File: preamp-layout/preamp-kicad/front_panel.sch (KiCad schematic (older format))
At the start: 14 parts, among them J13 Conn_01x02_Male, J14 Conn_01x02_Female, J46 Conn_01x04_Female, SW10 SW_Push_Open, SW11 SW_Push_Open, SW4 SW_Push_Open, SW5 SW_Push_Open, SW6 SW_Push_Open, SW7 SW_Push_Open, SW8 SW_Push_Open, SW9 SW_Push_Open, U4 4021

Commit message: AC PCB Update
Removed Switch symbol from PCB, moved to main sheet. Started playing with footprint assignment. Other minor updates.
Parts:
- renumbered J13 to J17, J14 to J18, J46 to J19
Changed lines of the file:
@@
 AR Path="/5E5EF2D4/60B80487" Ref="J?"  Part="1"
 AR Path="/6009D432/60B80487" Ref="J?"  Part="1"
-AR Path="/5E5ECAAE/60B80487" Ref="J13"  Part="1"
-F 0 "J13" H 1522 6428 50  0000 R CNN
+AR Path="/5E5ECAAE/60B80487" Ref="J17"  Part="1"
+F 0 "J17" H 1522 6428 50  0000 R CNN
 F 1 "Conn_01x02_Male" H 1522 6383 50  0001 R CNN
 F 2 "" H 1550 6500 50  0001 C CNN
@@
 P 1550 7050
 AR Path="/6009D432/60B804B3" Ref="J?"  Part="1"
-AR Path="/5E5ECAAE/60B804B3" Ref="J14"  Part="1"
-F 0 "J14" H 1578 6980 50  0000 L CNN
+AR Path="/5E5ECAAE/60B804B3" Ref="J18"  Part="1"
+F 0 "J18" H 1578 6980 50  0000 L CNN
 F 1 "Conn_01x02_Female" H 1578 6935 50  0001 L CNN
 F 2 "" H 1550 7050 50  0001 C CNN
@@
 NoConn ~ 10500 4050
 $Comp
-L Connector:Conn_01x04_Female J46
+L Connector:Conn_01x04_Female J19
 U 1 1 65AE66F9
 P 10150 2800
-F 0 "J46" H 10178 2730 50  0000 L CNN
+F 0 "J19" H 10178 2730 50  0000 L CNN
 F 1 "Conn_01x04_Female" H 10178 2685 50  0001 L CNN
 F 2 "" H 10150 2800 50  0001 C CNN

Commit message: Transformer specification
updated schematic, BOM with power transformer info. Other minor schematic tweaks.
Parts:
- removed J18: Conn_01x02_Female, symbol Connector:Conn_01x02_Female
- added J18: Conn_01x02_Male, Connector_JST:JST_EH_B2B-EH-A_1x02_P2.50mm_Vertical, symbol Connector:Conn_01x02_Male
- J17: footprint (none) -> Connector_JST:JST_EH_B2B-EH-A_1x02_P2.50mm_Vertical
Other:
- moved on the sheet: J19
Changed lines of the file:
@@
 L 4xxx:4021 U4
 U 1 1 639BBE1A
-P 10100 4550
-F 0 "U4" H 10100 5531 50  0000 C CNN
-F 1 "4021" H 10100 5440 50  0000 C CNN
-F 2 "" H 10100 4700 50  0001 C CNN
-F 3 "https://assets.nexperia.com/documents/data-sheet/HEF4021B.pdf" H 10100 4700 50  0001 C CNN
-	1    10100 4550
-	1    0    0    -1
-$EndComp
-Text GLabel 10100 3450 1    50   UnSpc ~ 0
-+5V
-Wire Wire Line
-	10100 3750 10100 3450
-Text Label 9550 4450 2    50   ~ 0
+P 9500 4400
+F 0 "U4" H 9500 5381 50  0000 C CNN
+F 1 "4021" H 9500 5290 50  0000 C CNN
+F 2 "" H 9500 4550 50  0001 C CNN
+F 3 "https://assets.nexperia.com/documents/data-sheet/HEF4021B.pdf" H 9500 4550 50  0001 C CNN
+	1    9500 4400
+	1    0    0    -1
+$EndComp
+Text GLabel 9500 3300 1    50   UnSpc ~ 0
++5V
+Wire Wire Line
+	9500 3600 9500 3300
+Text Label 8950 4300 2    50   ~ 0
 SW_CH1
-Text Label 9550 4550 2    50   ~ 0
+Text Label 8950 4400 2    50   ~ 0
 SW_CH2
-Text Label 9550 4650 2    50   ~ 0
+Text Label 8950 4500 2    50   ~ 0
 SW_CH3
-Text Label 9550 4750 2    50   ~ 0
+Text Label 8950 4600 2    50   ~ 0
 SW_CH4
-Text Label 9550 4850 2    50   ~ 0
+Text Label 8950 4700 2    50   ~ 0
 SW_CH5
-Text Label 9550 4950 2    50   ~ 0
+Text Label 8950 4800 2    50   ~ 0
 SW_MUTE
 Wire Wire Line
-	9700 4450 9550 4450
-Wire Wire Line
-	9550 4650 9700 4650
-Wire Wire Line
-	9550 4550 9700 4550
-Wire Wire Line
-	9700 4750 9550 4750
-Wire Wire Line
-	9700 4850 9550 4850
-Wire Wire Line
-	9700 4950 9550 4950
-Text HLabel 10650 4150 2    50   Output ~ 0
+	9100 4300 8950 4300
+Wire Wire Line
+	8950 4500 9100 4500
+Wire Wire Line
+	8950 4400 9100 4400
+Wire Wire Line
+	9100 4600 8950 4600
+Wire Wire Line
+	9100 4700 8950 4700
+Wire Wire Line
+	9100 4800 8950 4800
+Text HLabel 10050 4000 2    50   Output ~ 0
 MISO
-Text HLabel 9550 4250 0    50   Input ~ 0
+Text HLabel 8950 4100 0    50   Input ~ 0
 MOSI
-Text HLabel 9550 3950 0    50   Input ~ 0
+Text HLabel 8950 3800 0    50   Input ~ 0
 CLK
-Text HLabel 9550 4150 0    50   Input ~ 0
+Text HLabel 8950 4000 0    50   Input ~ 0
 CS
 Wire Wire Line
-	9550 4250 9700 4250
-Wire Wire Line
-	9550 4150 9700 4150
-Wire Wire Line
-	9550 3950 9700 3950
-Wire Wire Line
-	10500 4150 10650 4150
+	8950 4100 9100 4100
+Wire Wire Line
+	8950 4000 9100 4000
+Wire Wire Line
+	8950 3800 9100 3800
+Wire Wire Line
+	9900 4000 10050 4000
 Text Label 5150 2650 3    50   ~ 0
 SW_CH1
@@
 Text Label 7550 2650 3    50   ~ 0
 SW_OUT_2
-Text Label 9550 5050 2    50   ~ 0
+Text Label 8950 4900 2    50   ~ 0
 SW_OUT_1
-Text Label 9550 5150 2    50   ~ 0
+Text Label 8950 5000 2    50   ~ 0
 SW_OUT_2
 Wire Wire Line
-	9700 5050 9550 5050
-Wire Wire Line
-	9550 5150 9700 5150
+	9100 4900 8950 4900
+Wire Wire Line
+	8950 5000 9100 5000
 Text GLabel 2100 1800 1    50   UnSpc ~ 0
 +5V
@@
 F 0 "J17" H 1522 6428 50  0000 R CNN
 F 1 "Conn_01x02_Male" H 1522 6383 50  0001 R CNN
-F 2 "" H 1550 6500 50  0001 C CNN
+F 2 "Connector_JST:JST_EH_B2B-EH-A_1x02_P2.50mm_Vertical" H 1550 6500 50  0001 C CNN
 F 3 "~" H 1550 6500 50  0001 C CNN
 	1    1550 6500
@@
 Wire Wire Line
 	1350 7050 1150 7050
-$Comp
-L Connector:Conn_01x02_Female J?
-U 1 1 60B804B3
-P 1550 7050
-AR Path="/6009D432/60B804B3" Ref="J?"  Part="1"
-AR Path="/5E5ECAAE/60B804B3" Ref="J18"  Part="1"
-F 0 "J18" H 1578 6980 50  0000 L CNN
-F 1 "Conn_01x02_Female" H 1578 6935 50  0001 L CNN
-F 2 "" H 1550 7050 50  0001 C CNN
-F 3 "~" H 1550 7050 50  0001 C CNN
-	1    1550 7050
-	1    0    0    -1
-$EndComp
 $Comp
 L power:GND #PWR?
@@
 L power:GND #PWR?
 U 1 1 64EC7570
-P 10100 5350
+P 9500 5200
 AR Path="/5E26F6FE/64EC7570" Ref="#PWR?"  Part="1"
 AR Path="/5E5ECAAE/64EC7570" Ref="#PWR023"  Part="1"
-F 0 "#PWR023" H 10100 5100 50  0001 C CNN
-F 1 "GND" H 10105 5177 50  0000 C CNN
-F 2 "" H 10100 5350 50  0001 C CNN
-F 3 "" H 10100 5350 50  0001 C CNN
-	1    10100 5350
-	1    0    0    -1
-$EndComp
-NoConn ~ 10500 3950
-NoConn ~ 10500 4050
+F 0 "#PWR023" H 9500 4950 50  0001 C CNN
+F 1 "GND" H 9505 5027 50  0000 C CNN
+F 2 "" H 9500 5200 50  0001 C CNN
+F 3 "" H 9500 5200 50  0001 C CNN
+	1    9500 5200
+	1    0    0    -1
+$EndComp
+NoConn ~ 9900 3800
+NoConn ~ 9900 3900
 $Comp
 L Connector:Conn_01x04_Female J19
 U 1 1 65AE66F9
-P 10150 2800
-F 0 "J19" H 10178 2730 50  0000 L CNN
-F 1 "Conn_01x04_Female" H 10178 2685 50  0001 L CNN
-F 2 "" H 10150 2800 50  0001 C CNN
-F 3 "~" H 10150 2800 50  0001 C CNN
-	1    10150 2800
-	1    0    0    -1
-$EndComp
-Text HLabel 9950 2900 0    50   Output ~ 0
+P 9550 2650
+F 0 "J19" H 9578 2580 50  0000 L CNN
+F 1 "Conn_01x04_Female" H 9578 2535 50  0001 L CNN
+F 2 "" H 9550 2650 50  0001 C CNN
+F 3 "~" H 9550 2650 50  0001 C CNN
+	1    9550 2650
+	1    0    0    -1
+$EndComp
+Text HLabel 9350 2750 0    50   Output ~ 0
 MISO
-Text HLabel 9950 2700 0    50   Input ~ 0
+Text HLabel 9350 2550 0    50   Input ~ 0
 CLK
-Text HLabel 9950 2800 0    50   Input ~ 0
+Text HLabel 9350 2650 0    50   Input ~ 0
 MOSI
-Text HLabel 9950 3000 0    50   Input ~ 0
+Text HLabel 9350 2850 0    50   Input ~ 0
 CS
+$Comp
+L Connector:Conn_01x02_Male J?
+U 1 1 5E8B15E1
+P 1550 7050
+AR Path="/5E5EF2D4/5E8B15E1" Ref="J?"  Part="1"
+AR Path="/6009D432/5E8B15E1" Ref="J?"  Part="1"
+AR Path="/5E5ECAAE/5E8B15E1" Ref="J18"  Part="1"
+F 0 "J18" H 1522 6978 50  0000 R CNN
+F 1 "Conn_01x02_Male" H 1522 6933 50  0001 R CNN
+F 2 "Connector_JST:JST_EH_B2B-EH-A_1x02_P2.50mm_Vertical" H 1550 7050 50  0001 C CNN
+F 3 "~" H 1550 7050 50  0001 C CNN
+	1    1550 7050
+	-1   0    0    -1
+$EndComp
 $EndSCHEMATC

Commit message: Added front panel LED sheet. BOM update. Front panel PCA work
other minor changes like LED color assignments, etc
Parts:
- removed D12, D13: WS2812B, LED_SMD:LED_WS2812B_PLCC4_5.0x5.0mm_P3.2mm, symbol LED:WS2812B
- removed J19: Conn_01x04_Female, symbol Connector:Conn_01x04_Female
- removed SW10, SW11, SW4, SW5, SW6, SW7, SW8, SW9: SW_Push_Open, symbol Switch:SW_Push_Open
- removed U4: 4021, symbol 4xxx:4021
- added C37, C38, C39, C40, C41, C42, C43, C44: 0.1uF, Capacitor_SMD:C_1206_3216Metric_Pad1.42x1.75mm_HandSolder, symbol Device:C
- added D60: RED, LED_SMD:LED_1206_3216Metric_Pad1.42x1.75mm_HandSolder, symbol Device:LED
- added J19: Conn_01x05_Female, symbol Connector:Conn_01x05_Female
- added J72, J73, J74, J75, J76, J77, J78, J79: Conn_01x03_Female, Connector_PinHeader_2.54mm:PinHeader_1x03_P2.54mm_Vertical, symbol Connector:Conn_01x03_Female
- added R87, R88, R89, R90, R91, R92, R93, R94: 100R, Resistor_SMD:R_1206_3216Metric_Pad1.42x1.75mm_HandSolder, symbol Device:R
- added R95: 430, Resistor_SMD:R_1206_3216Metric_Pad1.42x1.75mm_HandSolder, symbol Device:R
- added U4: MC33978, symbol preamp:MC33978
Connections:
- net labels added: SW_1, SW_2, SW_3, SW_4, SW_5, SW_6, SW_7, SW_8, SW_INT, SW_IN_1, SW_IN_2, SW_IN_3, SW_IN_4, SW_IN_5
- net labels removed: LED_DT, SW_CH1, SW_CH2, SW_CH3, SW_CH4, SW_CH5
- wire segments 21 -> 122
- no-connect marks 2 -> 16
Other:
- moved on the sheet: J17, J18

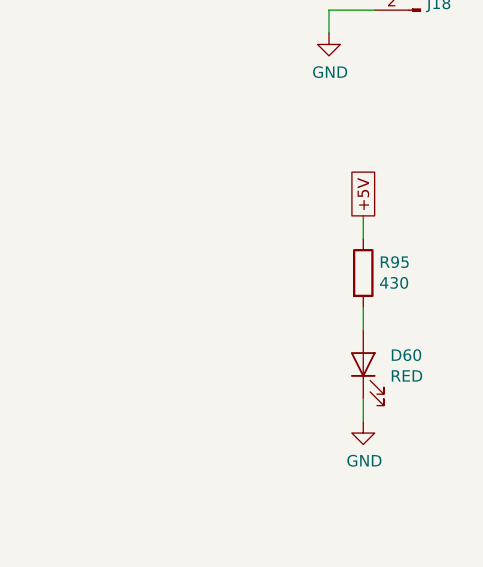
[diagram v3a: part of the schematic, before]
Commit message: LED resistor update
In the process of reviewing layouts and associated parts sourcing, I realized that I had incorrectly calculated the resistors needed for the power supply LEDs on all boards. Updated BOM and schematics to match. Other minor schematic updates.
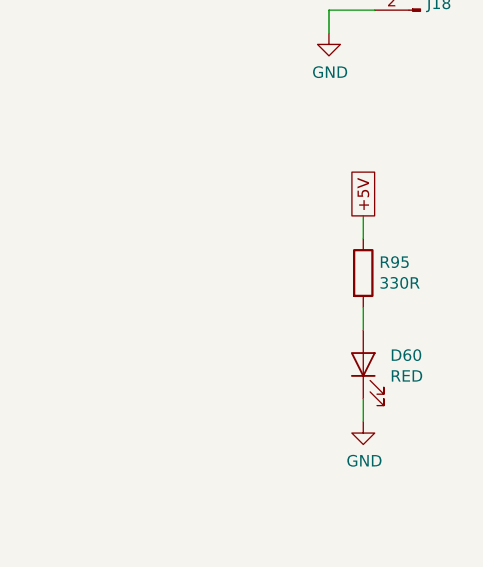
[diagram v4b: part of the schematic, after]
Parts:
- R95: value 430 -> 330R
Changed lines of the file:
@@
 Connection ~ 3600 5950
-$Comp
-L Device:R R?
-U 1 1 5ECB89C1
-P 9650 4600
-AR Path="/5E2D8DA2/5ECB89C1" Ref="R?"  Part="1"
-AR Path="/5ECB89C1" Ref="R?"  Part="1"
-AR Path="/5E27B612/5ECB89C1" Ref="R?"  Part="1"
-AR Path="/5E5EF2D4/5ECB89C1" Ref="R?"  Part="1"
-AR Path="/5E5ECAAE/5ECB89C1" Ref="R95"  Part="1"
-F 0 "R95" H 9720 4646 50  0000 L CNN
-F 1 "430" H 9720 4555 50  0000 L CNN
-F 2 "Resistor_SMD:R_1206_3216Metric_Pad1.42x1.75mm_HandSolder" V 9580 4600 50  0001 C CNN
-F 3 "~" H 9650 4600 50  0001 C CNN
-	1    9650 4600
-	1    0    0    -1
-$EndComp
 $Comp
 L Device:LED D?
@@
 Wire Wire Line
 	3600 5750 3600 5950
+$Comp
+L Device:R R?
+U 1 1 5ECB89C1
+P 9650 4600
+AR Path="/5E2D8DA2/5ECB89C1" Ref="R?"  Part="1"
+AR Path="/5ECB89C1" Ref="R?"  Part="1"
+AR Path="/5E27B612/5ECB89C1" Ref="R?"  Part="1"
+AR Path="/5E5EF2D4/5ECB89C1" Ref="R?"  Part="1"
+AR Path="/5E5ECAAE/5ECB89C1" Ref="R95"  Part="1"
+F 0 "R95" H 9720 4646 50  0000 L CNN
+F 1 "330R" H 9720 4555 50  0000 L CNN
+F 2 "Resistor_SMD:R_1206_3216Metric_Pad1.42x1.75mm_HandSolder" V 9580 4600 50  0001 C CNN
+F 3 "~" H 9650 4600 50  0001 C CNN
+	1    9650 4600
+	1    0    0    -1
+$EndComp
 $EndSCHEMATC

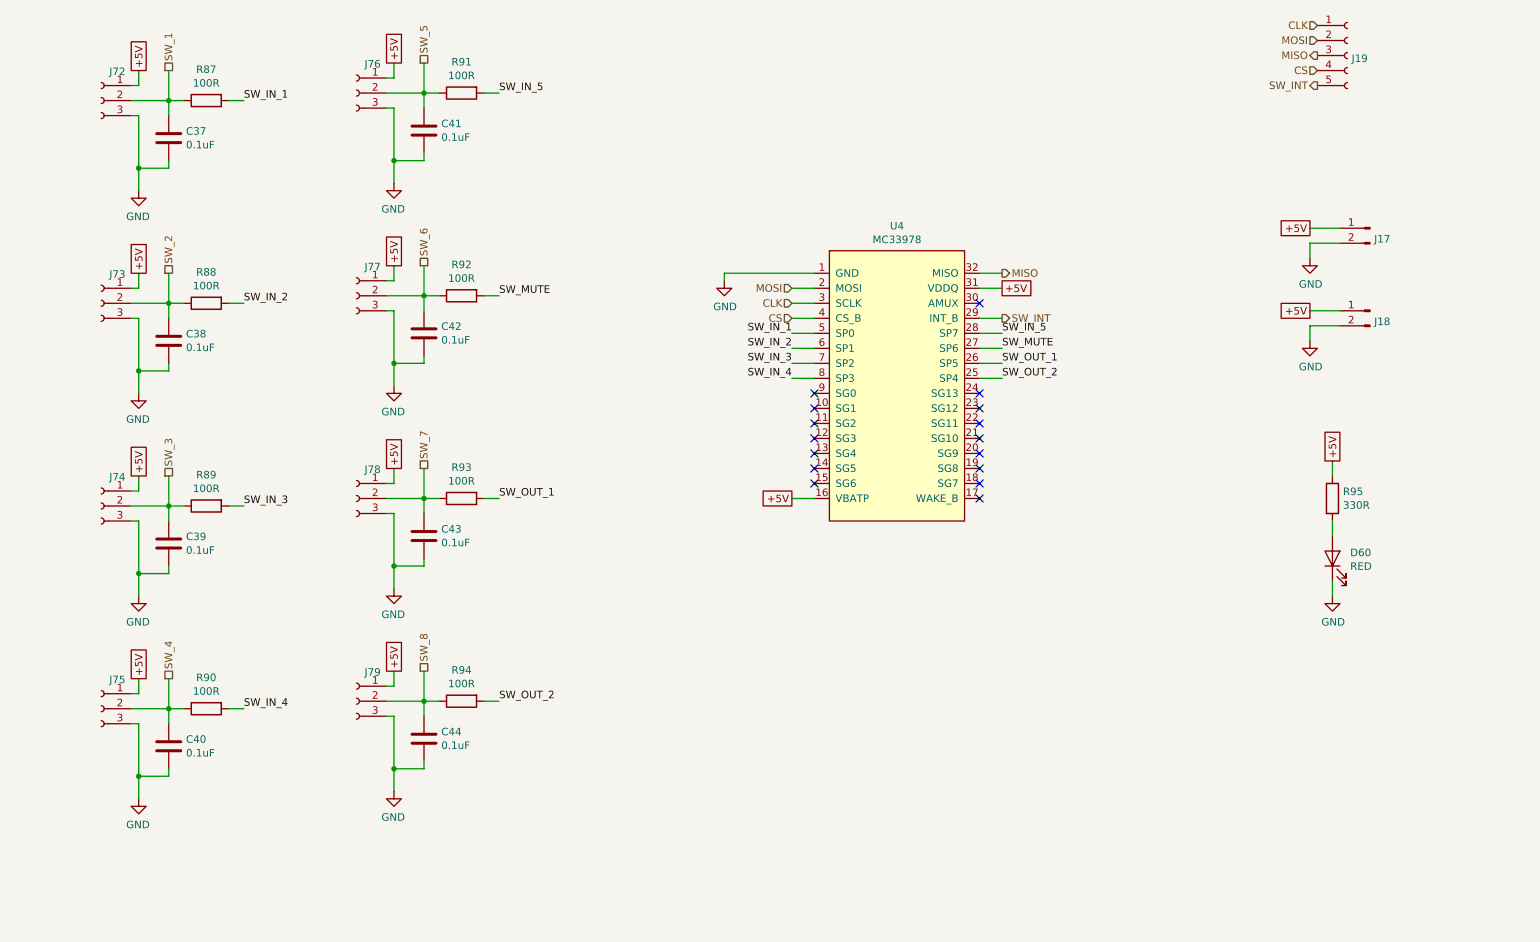
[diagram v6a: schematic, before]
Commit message: BOM Update
parts added to BOM, connector cleanup. Stopping point before renumbering refdes in a more intelligent way.
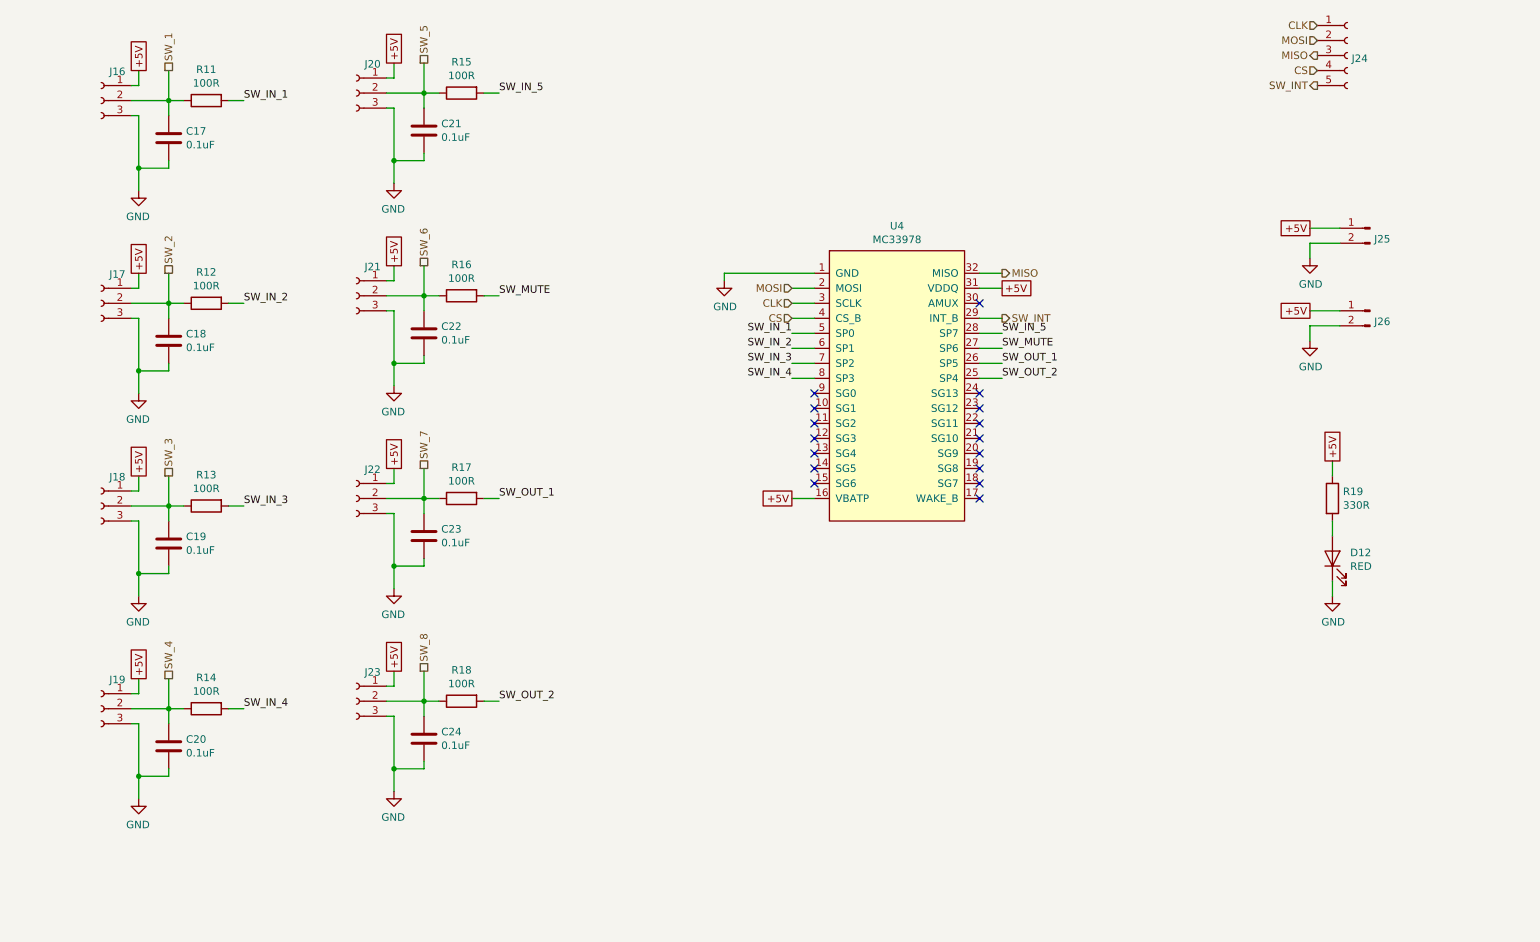
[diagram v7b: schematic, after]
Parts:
- renumbered C37 to C17, C38 to C18, C39 to C19, C40 to C20, C41 to C21, C42 to C22, C43 to C23, C44 to C24, D60 to D12, J72 to J16, J73 to J17, J74 to J18, J75 to J19, J76 to J20, J77 to J21, J78 to J22, J79 to J23, J19 to J24, J17 to J25, J18 to J26, R87 to R11, R88 to R12, R89 to R13, R90 to R14, R91 to R15, R92 to R16, R93 to R17, R94 to R18, R95 to R19

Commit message: Footprint updates
Footprint creation of relay, ESP32
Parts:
- J24: footprint (none) -> Connector_PinHeader_2.54mm:PinHeader_1x05_P2.54mm_Vertical
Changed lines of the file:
@@
 F 0 "J24" H 9778 1630 50  0000 L CNN
 F 1 "Conn_01x05_Female" H 9778 1585 50  0001 L CNN
-F 2 "" H 9750 1650 50  0001 C CNN
+F 2 "Connector_PinHeader_2.54mm:PinHeader_1x05_P2.54mm_Vertical" H 9750 1650 50  0001 C CNN
 F 3 "~" H 9750 1650 50  0001 C CNN
 	1    9750 1650
